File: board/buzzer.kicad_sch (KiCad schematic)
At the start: 0 parts

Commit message: add: Hierarchical Sheets
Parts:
- added BZ1: Buzzer, Buzzer_Beeper:MagneticBuzzer_PUI_AT-0927-TT-6-R, symbol Device:Buzzer
- added C4, C6: 10n, Capacitor_SMD:C_0603_1608Metric, symbol Device:C
- added C9: 100n, Capacitor_SMD:C_0603_1608Metric, symbol Device:C
- added Q2: Q_NPN_BEC, Package_TO_SOT_SMD:SOT-23, symbol Transistor_BJT:Q_NPN_BEC
- added R19: 1k, Resistor_SMD:R_0603_1608Metric, symbol Device:R_US
- added R20: 470, Resistor_SMD:R_0603_1608Metric, symbol Device:R_US
- added RV2: 10k, Potentiometer_THT:Potentiometer_Piher_PT-6-V_Vertical, symbol Device:R_Potentiometer_US
- added U5: NE555D, Package_SO:SOIC-8_3.9x4.9mm_P1.27mm, symbol Timer:NE555D
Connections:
- new net: BZ1.2 (-), Q2.3 (C)
- new net: Q2.1 (B), R20.1
- new net: R20.2, U5.3 (Q)
- new net: C4.1, R19.1, RV2.3, U5.2 (TR), U5.7 (DIS)
- new net: R19.2, U5.6 (THR)
- new net: C6.2, U5.5 (CV)
- new net 5V: BZ1.1 (+), C9.1, RV2.1, RV2.2, U5.8 (VCC)
- new net ALARM: U5.4 (R)
- new net GND: C4.2, C6.1, C9.2, Q2.2 (E), U5.1 (GND)

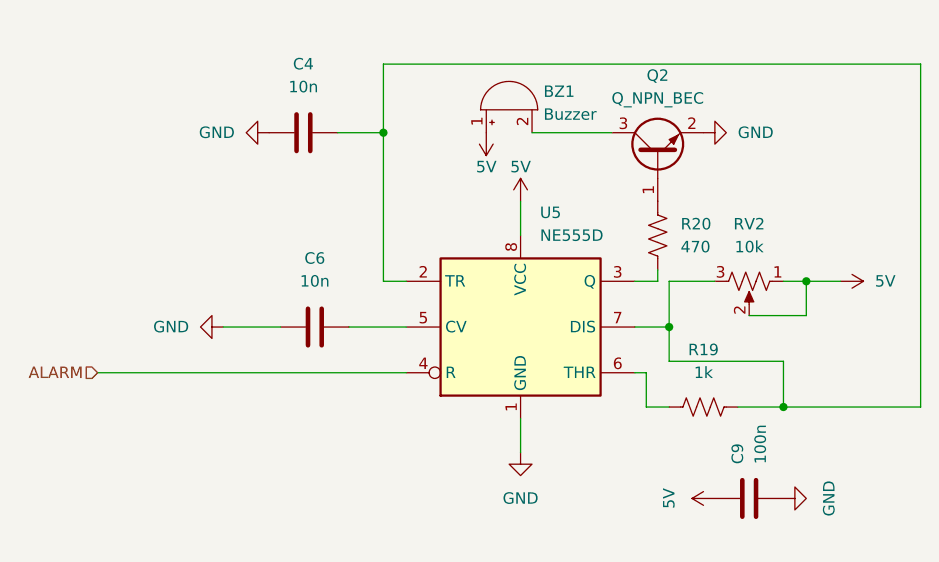
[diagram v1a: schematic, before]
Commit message: add: Mounting holes, box comments
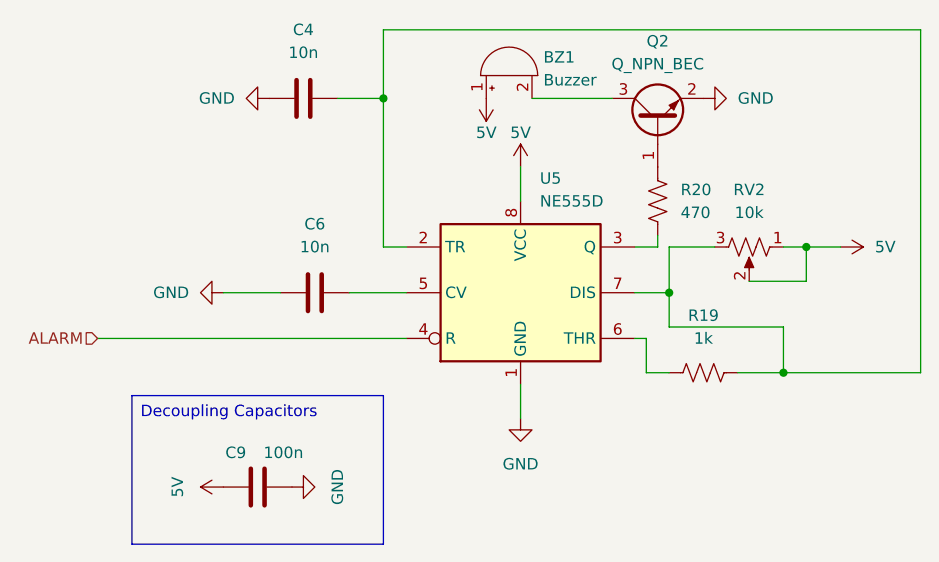
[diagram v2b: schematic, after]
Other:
- moved on the sheet: BZ1, C4, C6, C9, Q2, R19, R20, RV2, U5
